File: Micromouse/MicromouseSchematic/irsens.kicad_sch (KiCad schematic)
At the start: 28 parts, among them J6 IR_1, J7 IR_2, J8 IR_3, J9 IR_4, Q2 DMN3065LW-7, Q3 DMN3065LW-7, Q4 DMN3065LW-7, Q5 DMN3065LW-7

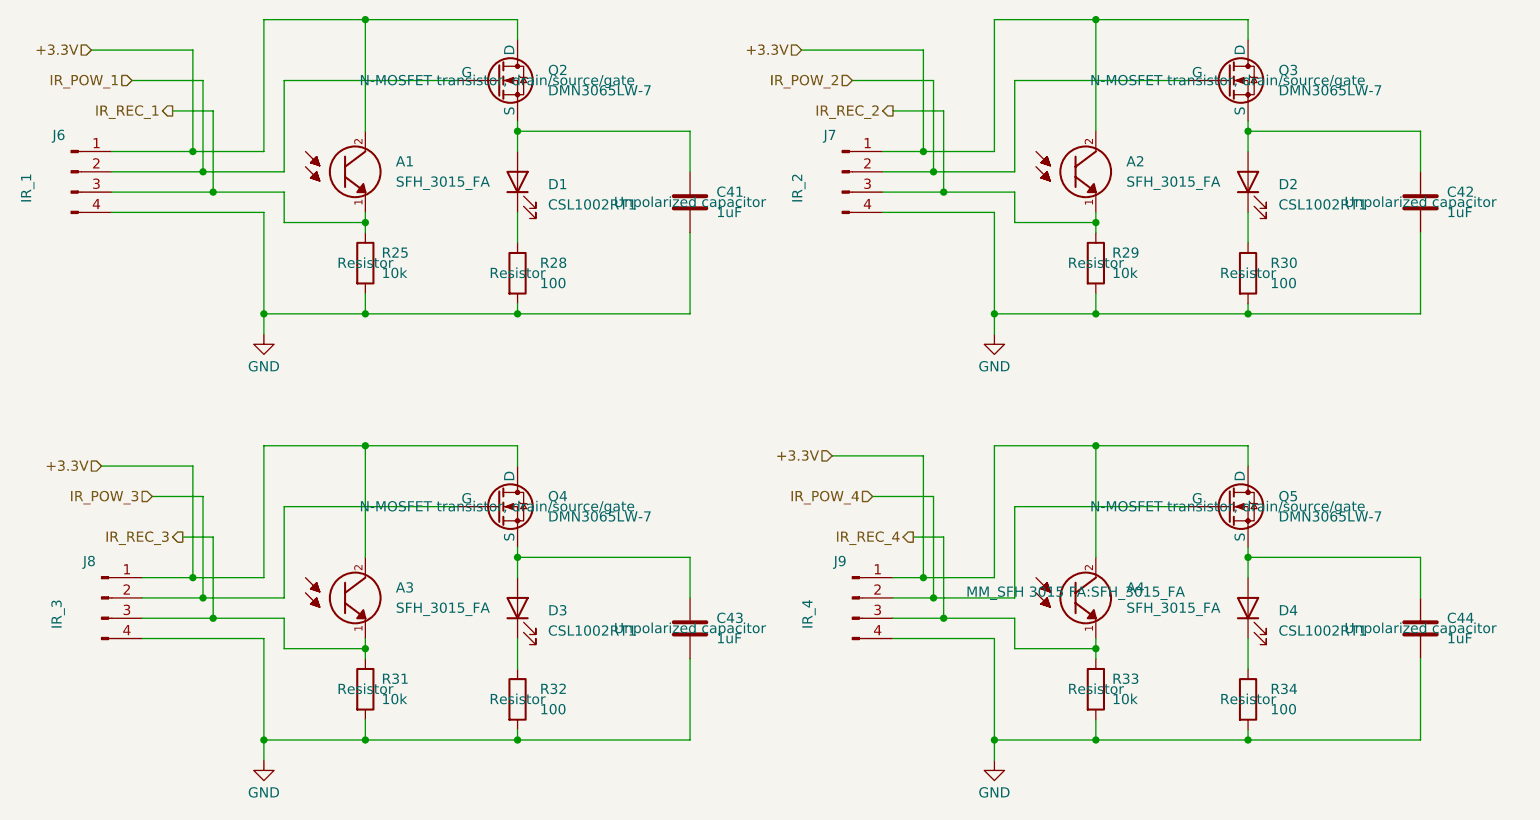
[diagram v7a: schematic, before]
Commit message: Changd IR sensors and emmiters to 5mm LEDs
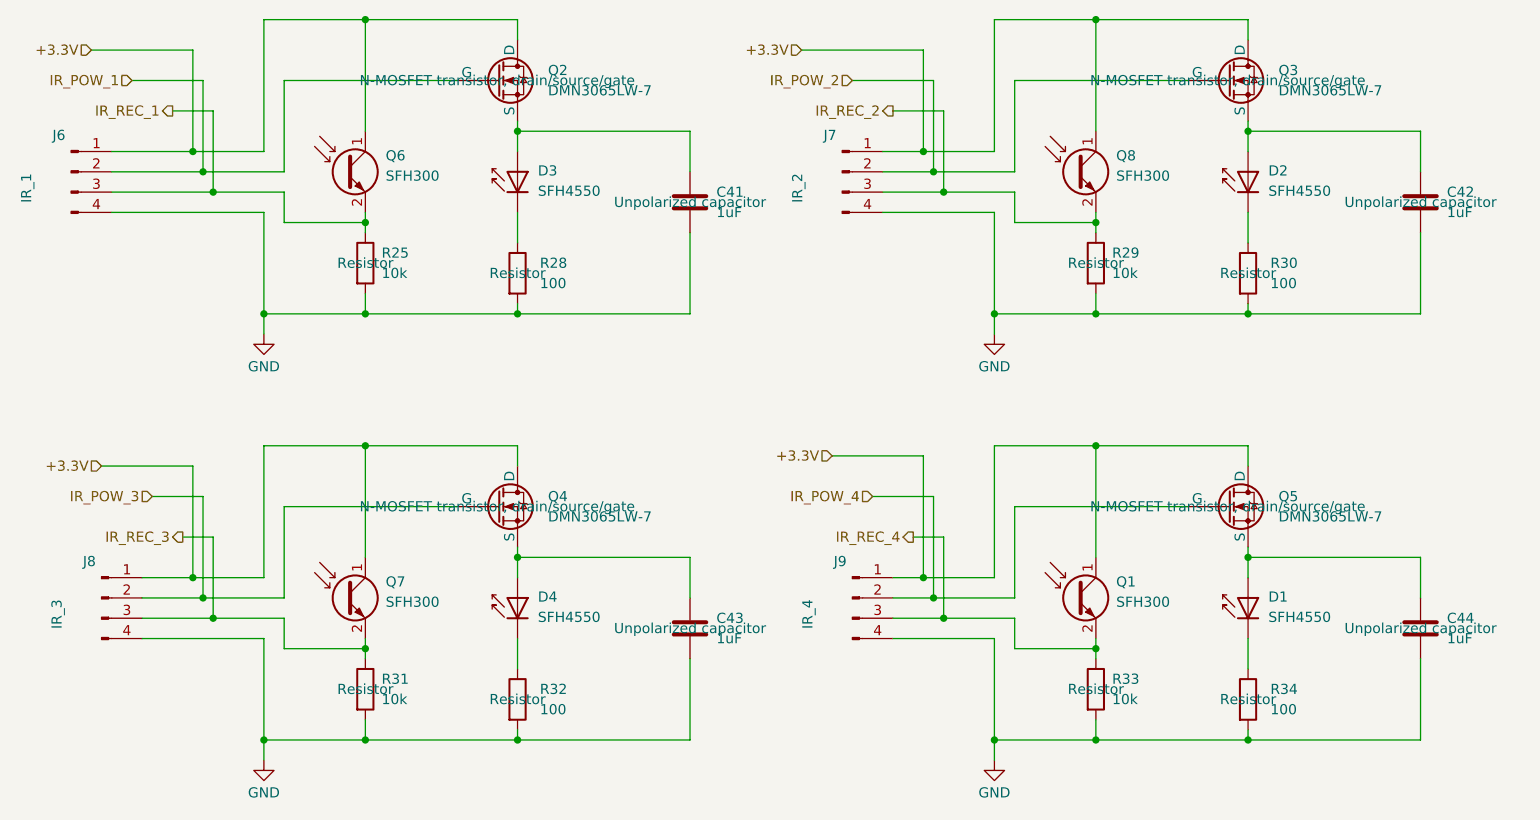
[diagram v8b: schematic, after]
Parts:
- removed A1, A2, A3, A4: SFH_3015_FA, MM_SFH 3015 FA:SFH_3015_FA, symbol SFH_3015_FA:SFH_3015_FA
- removed D1, D2, D3, D4: CSL1002RT1, symbol Device:LED
- added D1, D2, D3, D4: SFH4550, LED_THT:LED_D5.0mm_IRGrey, symbol LED:SFH4550
- added Q1, Q6, Q7, Q8: SFH300, LED_THT:LED_D5.0mm_Clear, symbol Sensor_Optical:SFH300
- C41, C42, C43, C44: footprint (none) -> Capacitor_SMD:C_0402_1005Metric
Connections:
- net +3.3V: now also Q1.1 (C), Q6.1 (C), Q7.1 (C), Q8.1 (C)
- net IR_REC_1: now also Q6.2 (E)
- net IR_REC_2: now also Q8.2 (E)
- net IR_REC_3: now also Q7.2 (E)
- net IR_REC_4: now also Q1.2 (E)
- net at C43.1, Q4.3 (S): now also D4.2 (A)
- net at C44.1, Q5.3 (S): now also D1.2 (A)
- net at R34.1: now also D1.1 (K)
- net at R28.1: now also D3.1 (K)
- net at C41.1, Q2.3 (S): now also D3.2 (A)
- net at C42.1, Q3.3 (S): now also D2.2 (A)
- net at R32.1: now also D4.1 (K)
- net at R30.1: now also D2.1 (K)
